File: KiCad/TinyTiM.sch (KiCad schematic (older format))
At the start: 34 parts, among them P101 PWR_NW, P102 DO_N1, P103 DO_N2, P104 DI_N1, P105 DI_N2, P106 PWR_NE, P107 PWR_W, P108 PWR_E, P109 DI_W2, P110 DO_E2, P111 DI_W1, P112 DO_E1, P113 PWR_SW, P114 DI_S1, P115 DI_S2, P116 DO_S1, P117 DO_S2, P118 PWR_SE, P119 DO_H_SER, P120 DI_A_SER, P121 DI_A_SER, P122 DO_H_SER, P123 DI_A_Ser, P124 DO_H_Ser, P125 G>H, P126 F>G, P127 E>F, P128 D>E, P129 C>D, P130 B>C, P131 A>B

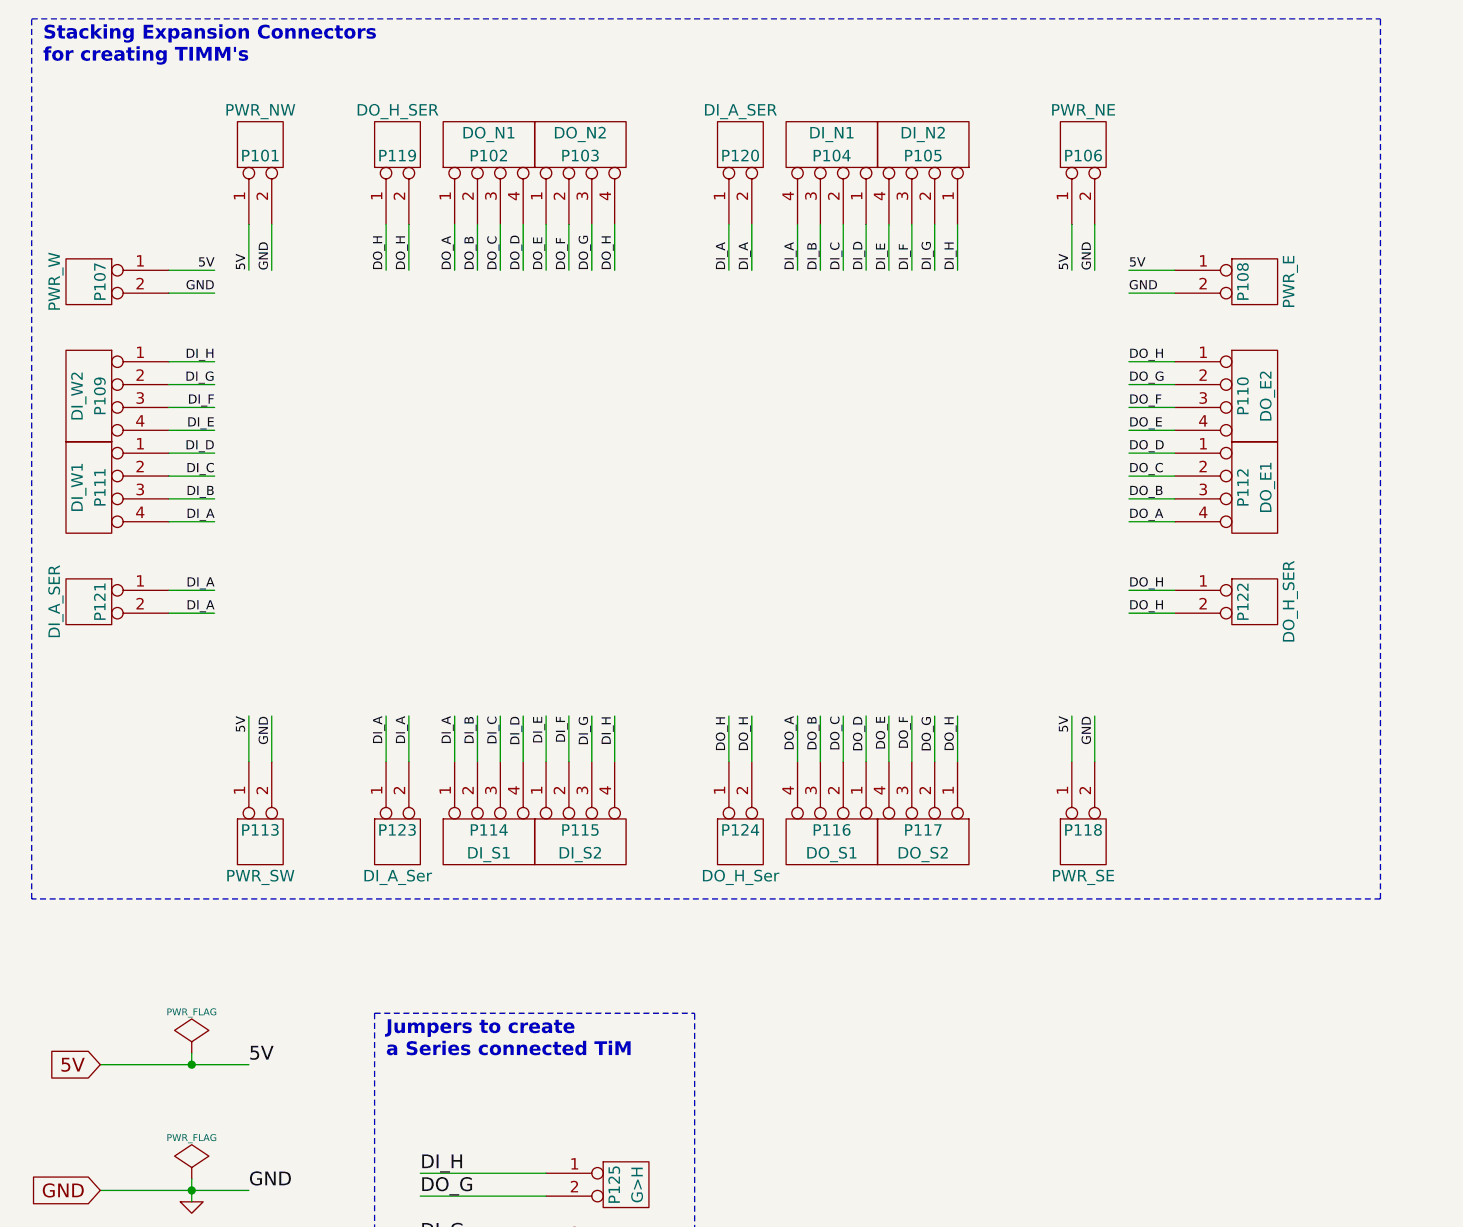
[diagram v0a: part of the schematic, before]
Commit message: TinyTiM KiCad work in progress
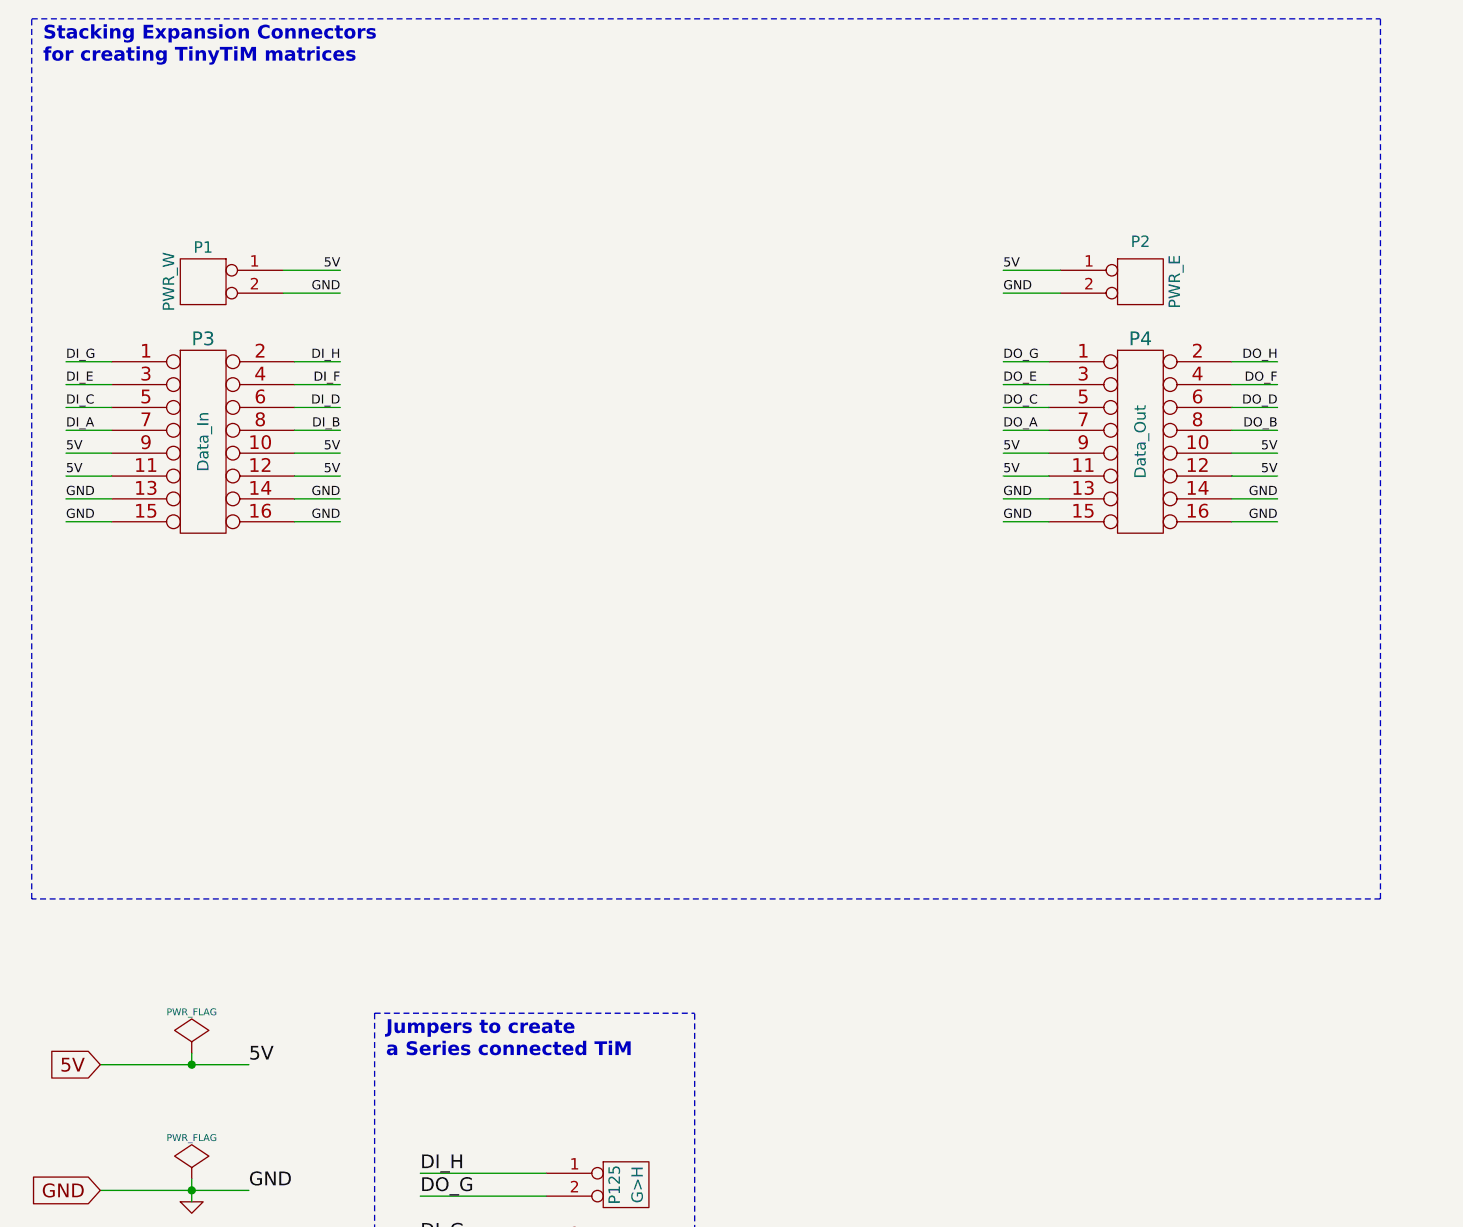
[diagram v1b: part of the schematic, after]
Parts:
- removed P101: PWR_NW, SIL-PWR-2, symbol CONN_2
- removed P102: DO_N1, CONN_S, symbol CONN_N
- removed P103: DO_N2, CONN_S, symbol CONN_N
- removed P104: DI_N1, CONN_N, symbol CONN_N
- removed P105: DI_N2, CONN_N, symbol CONN_N
- removed P106: PWR_NE, SIL-PWR-2, symbol CONN_2
- removed P109: DI_W2, CONN_N, symbol CONN_W
- removed P110: DO_E2, CONN_S, symbol CONN_E
- removed P111: DI_W1, CONN_N, symbol CONN_W
- removed P112: DO_E1, CONN_S, symbol CONN_E
- removed P113: PWR_SW, SIL-PWR, symbol CONN_2
- removed P114: DI_S1, CONN_N, symbol CONN4_S
- removed P115: DI_S2, CONN_N, symbol CONN4_S
- removed P116: DO_S1, CONN_S, symbol CONN4_S
- removed P117: DO_S2, CONN_S, symbol CONN4_S
- removed P118: PWR_SE, SIL-PWR, symbol CONN_2
- removed P119, P122: DO_H_SER, SIL-PWR-2, symbol CONN_2
- removed P120: DI_A_SER, SIL-PWR-2, symbol CONN_2
- removed P121: DI_A_SER, SIL-PWR, symbol CONN_2
- removed P123: DI_A_Ser, SIL-PWR, symbol CONN_2
- removed P124: DO_H_Ser, SIL-PWR, symbol CONN_2
- added P3: Data_In, symbol CONN_8X2
- added P4: Data_Out, symbol CONN_8X2
- L101: footprint OSHW_6mm -> TinyTiM_Lib:OSHW_6mm
- L102: footprint Logo-WL3 -> TinyTiM_Lib:Logo-WL3
- P1: renamed from P107; footprint SIL-PWR -> TinyTiM_Lib:SIL-PWR
- P125, P126, P127, P128, P129, P130, P131: footprint ShortLink2 -> TinyTiM_Lib:ShortLink2
- P2: renamed from P108; footprint SIL-PWR-2 -> TinyTiM_Lib:SIL-PWR
- PCB101: footprint PCB -> TinyTiM_Lib:PCB
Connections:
- net 5V: now also P3.10, P3.11, P3.12, P3.9, P4.10, P4.11, P4.12, P4.9
- net DI_A: now also P3.7
- net DI_B: now also P3.8
- net DI_C: now also P3.5
- net DI_D: now also P3.6
- net DI_E: now also P3.3
- net DI_F: now also P3.4
- net DI_G: now also P3.1
- net DI_H: now also P3.2
- net DO_A: now also P4.7
- net DO_B: now also P4.8
- net DO_C: now also P4.5
- net DO_D: now also P4.6
- net DO_E: now also P4.3
- net DO_F: now also P4.4
- net DO_G: now also P4.1
- net DO_H: now also P4.2
- net GND: now also P3.13, P3.14, P3.15, P3.16, P4.13, P4.14, P4.15, P4.16
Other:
- note added: "Stacking Expansion Connectors\nfor creating TinyTiM matrices"
- note removed: "Stacking Expansion Connectors\nfor creating TIMM's"
- moved on the sheet: P1, P2

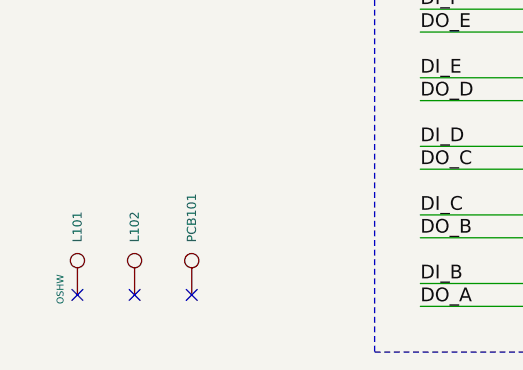
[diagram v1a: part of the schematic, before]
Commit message: TinyTiM KiCad work in progress
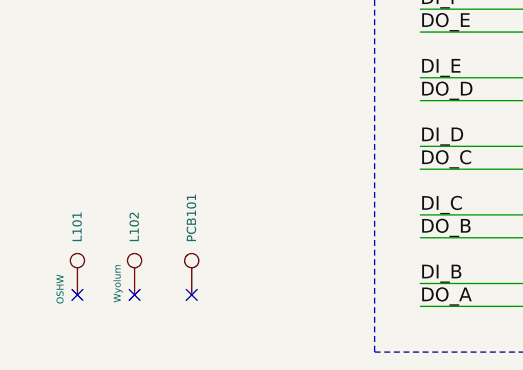
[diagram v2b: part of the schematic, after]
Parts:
- P1, P2: footprint TinyTiM_Lib:SIL-PWR -> TinyTiM_Lib:Conn_x2_PTSM
- P3, P4: footprint (none) -> TinyTiM_Lib:Header_8x2
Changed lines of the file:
@@
 01 31 04 0B 88 21 58 40 0C C1 02 62 08 16 10 43 B0 80 18 82 05 C4 10 2C 20 86 60 01 31 04 0B 88
 21 58 40 0C C1 02 62 08 16 10 43 B0 80 18 82 05 C4 10 2C 20 86 60 01 31 04 0B 88 21 58 40 0C C1
-02 62 7C 03 3D 79 5E 0E 30 13 47 E7 00 00 00 00 49 45 4E 44 AE 42 60 82 20
+02 62 7C 03 3D 79 5E 0E 30 13 47 E7 00 00 00 00 49 45 4E 44 AE 42 60 82 30
 EndData
 $EndBitmap
@@
 C1 ED 35 72 E0 F7 FB FF F1 1F FF F1 9F FF F9 9F C7 C7 C7 73 1A 9F 2B 70 38 1C FB F6 ED 3B 79 F2
 E4 23 8F 3C 52 B0 F1 D9 2E 76 F1 FF 03 17 ED 19 47 28 92 59 FB 00 00 00 00 49 45 4E 44 AE 42 60
-82 F4
+82 91
 EndData
 $EndBitmap
@@
 P 1050 7350
 F 0 "L102" H 1130 7350 40  0000 L CNN
-F 1 "Wyolum" H 1050 7405 30  0001 C CNN
+F 1 "Wyolum" H 950 7425 30  0000 C CNN
 F 2 "TinyTiM_Lib:Logo-WL3" H 975 7425 30  0001 C CNN
 F 3 "" H 1050 7350 60  0001 C CNN
@@
 F 0 "P2" H 5450 1925 50  0000 C CNN
 F 1 "PWR_E" V 5600 1750 50  0000 C CNN
-F 2 "TinyTiM_Lib:SIL-PWR" V 5600 1750 50  0001 C CNN
+F 2 "TinyTiM_Lib:Conn_x2_PTSM" V 5600 1750 50  0001 C CNN
 F 3 "" H 5450 1750 60  0001 C CNN
 F 4 "CONN HEADER 50POS .100\" SGL GOLD" H 5450 1850 60  0001 L CNN "Field4"
@@
 F 0 "P1" H 1350 1900 50  0000 C CNN
 F 1 "PWR_W" V 1500 1750 50  0000 C CNN
-F 2 "TinyTiM_Lib:SIL-PWR" V 1500 1750 50  0001 C CNN
+F 2 "TinyTiM_Lib:Conn_x2_PTSM" V 1500 1750 50  0001 C CNN
 F 3 "" H 1350 1750 60  0001 C CNN
 F 4 "CONN HEADER 50POS .100\" SGL GOLD" H 1350 1850 60  0001 L CNN "Field4"
@@
 F 0 "P3" H 1350 2900 60  0000 C CNN
 F 1 "Data_In" V 1350 2450 50  0000 C CNN
-F 2 "" H 1350 2450 60  0001 C CNN
+F 2 "TinyTiM_Lib:Header_8x2" H 1350 2450 60  0001 C CNN
 F 3 "" H 1350 2450 60  0000 C CNN
 	1    1350 2450
@@
 F 0 "P4" H 5450 2900 60  0000 C CNN
 F 1 "Data_Out" V 5450 2450 50  0000 C CNN
-F 2 "" H 5450 2450 60  0001 C CNN
+F 2 "TinyTiM_Lib:Header_8x2" H 5450 2450 60  0001 C CNN
 F 3 "" H 5450 2450 60  0000 C CNN
 	1    5450 2450

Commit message: KiCad work in progress
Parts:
- added P5: Data_In_Serial, Conn_x3_PTSM, symbol CONN_3
- added P6: Data_Out_Serial, Conn_x3_PTSM, symbol CONN_3
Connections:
- net 5V: now also P5.2 (P2), P6.2 (P2)
- net DI_A: now also P5.3 (P3)
- net DO_H: now also P6.3 (P3)
- net GND: now also P5.1 (P1), P6.1 (P1)
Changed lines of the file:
@@
 LIBS:power
 LIBS:TinyTiM-cache
-EELAYER 24 0
+EELAYER 27 0
 EELAYER END
 $Descr A4 11693 8268
@@
 Sheet 1 9
 Title "TiM - The Intelligent Matrix"
-Date "16 feb 2013"
+Date "24 apr 2014"
 Rev ""
 Comp "WyoLum"
@@
 01 31 04 0B 88 21 58 40 0C C1 02 62 08 16 10 43 B0 80 18 82 05 C4 10 2C 20 86 60 01 31 04 0B 88
 21 58 40 0C C1 02 62 08 16 10 43 B0 80 18 82 05 C4 10 2C 20 86 60 01 31 04 0B 88 21 58 40 0C C1
-02 62 7C 03 3D 79 5E 0E 30 13 47 E7 00 00 00 00 49 45 4E 44 AE 42 60 82 30
+02 62 7C 03 3D 79 5E 0E 30 13 47 E7 00 00 00 00 49 45 4E 44 AE 42 60 82 F1 $EndBitmap
 EndData
 $EndBitmap
@@
 C1 ED 35 72 E0 F7 FB FF F1 1F FF F1 9F FF F9 9F C7 C7 C7 73 1A 9F 2B 70 38 1C FB F6 ED 3B 79 F2
 E4 23 8F 3C 52 B0 F1 D9 2E 76 F1 FF 03 17 ED 19 47 28 92 59 FB 00 00 00 00 49 45 4E 44 AE 42 60
-82 91
+82 37 $EndBitmap
 EndData
 $EndBitmap
@@
 P 1350 1750
 F 0 "P1" H 1350 1900 50  0000 C CNN
-F 1 "PWR_W" V 1500 1750 50  0000 C CNN
+F 1 "PWR_W" H 1350 1600 50  0000 C CNN
 F 2 "TinyTiM_Lib:Conn_x2_PTSM" V 1500 1750 50  0001 C CNN
 F 3 "" H 1350 1750 60  0001 C CNN
@@
 U 1 1 5355499C
 P 1350 2450
-F 0 "P3" H 1350 2900 60  0000 C CNN
-F 1 "Data_In" V 1350 2450 50  0000 C CNN
+F 0 "P3" H 1350 2900 50  0000 C CNN
+F 1 "Data_In" H 1350 2000 50  0000 C CNN
 F 2 "TinyTiM_Lib:Header_8x2" H 1350 2450 60  0001 C CNN
 F 3 "" H 1350 2450 60  0000 C CNN
@@
 Text Label 6050 2800 2    40   ~ 0
 GND
+Text Label 1900 3350 2    40   ~ 0
+DI_A
+Wire Wire Line
+	1900 3350 1700 3350
+Wire Wire Line
+	1700 3550 1900 3550
+Text Label 1900 3550 2    40   ~ 0
+GND
+Wire Wire Line
+	1700 3450 1900 3450
+Text Label 1900 3450 2    40   ~ 0
+5V
+$Comp
+L CONN_3 P5
+U 1 1 5358CE5E
+P 1350 3450
+F 0 "P5" H 1350 3250 50  0000 C CNN
+F 1 "Data_In_Serial" H 1350 3650 50  0000 C CNN
+F 2 "Conn_x3_PTSM" H 1350 3400 60  0001 C CNN
+F 3 "" H 1350 3400 60  0000 C CNN
+F 4 "CONN HEADER 50POS .100\" SGL GOLD" H 1350 3500 60  0001 L CNN "Field4"
+F 5 "Header, Unshrouded, Male pin," H 1350 3600 60  0001 L CNN "Field5"
+F 6 "0.1\"" H 1350 3700 60  0001 L CNN "Field6"
+	1    1350 3450
+	-1   0    0    1
+$EndComp
+Text Label 4900 3350 0    40   ~ 0
+DO_H
+Wire Wire Line
+	4900 3350 5100 3350
+Wire Wire Line
+	5100 3550 4900 3550
+Text Label 4900 3550 0    40   ~ 0
+GND
+Wire Wire Line
+	5100 3450 4900 3450
+Text Label 4900 3450 0    40   ~ 0
+5V
+$Comp
+L CONN_3 P6
+U 1 1 5358D167
+P 5450 3450
+F 0 "P6" H 5450 3250 50  0000 C CNN
+F 1 "Data_Out_Serial" H 5450 3650 50  0000 C CNN
+F 2 "Conn_x3_PTSM" H 5450 3400 60  0001 C CNN
+F 3 "" H 5450 3400 60  0000 C CNN
+F 4 "CONN HEADER 50POS .100\" SGL GOLD" H 5450 3500 60  0001 L CNN "Field4"
+F 5 "Header, Unshrouded, Male pin," H 5450 3600 60  0001 L CNN "Field5"
+F 6 "0.1\"" H 5450 3700 60  0001 L CNN "Field6"
+	1    5450 3450
+	1    0    0    1
+$EndComp
 $EndSCHEMATC
